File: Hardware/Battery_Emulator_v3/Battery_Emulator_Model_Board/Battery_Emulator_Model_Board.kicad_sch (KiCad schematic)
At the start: 43 parts, among them J1 Vin, J10 Conn_01x05, J11 Conn_01x05, J12 Conn_01x05, J13 Conn_01x05, J14 Conn_01x05, J15 Conn_01x05, J16 Conn_01x05, J17 Conn_01x05, J2 USB4105-GF-A-060, J3 Conn_01x05, J5 Conn_01x05, J6 Conn_01x05, J7 Conn_01x05, J8 Conn_01x05, J9 Conn_01x05, U1 ATmega328PB-A, U2 KA78M05_TO252, U3 FT230XS-R, U4 74AHC2G125DP,125, Y1 Crystal_GND24

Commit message: Hardware Update
Finished the Model Board PCB
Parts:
- added TP4: GND, TestPoint:TestPoint_Pad_D2.5mm, symbol Connector:TestPoint
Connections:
- net GND: now also TP4.1
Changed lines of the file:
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@@
   (junction (at 49.53 21.59) (diameter 0) (color 0 0 0 0)
   )
+  (junction (at 107.315 36.83) (diameter 0) (color 0 0 0 0)
+  )
   (junction (at 77.47 113.03) (diameter 0) (color 0 0 0 0)
   )
@@
         )
       )
+    )
+  )
+  (symbol (lib_id "Connector:TestPoint") (at 107.315 36.83 180) (unit 1)
+    (in_bom yes) (on_board yes) (dnp no) (fields_autoplaced)
+    (property "Reference" "TP4" (at 109.855 38.862 0)
+      (effects (font (size 1.27 1.27)) (justify right))
+    )
+    (property "Value" "GND" (at 109.855 41.402 0)
+      (effects (font (size 1.27 1.27)) (justify right))
+    )
+    (property "Footprint" "TestPoint:TestPoint_Pad_D2.5mm" (at 102.235 36.83 0)
+      (effects (font (size 1.27 1.27)) hide)
+    )
+    (property "Datasheet" "~" (at 102.235 36.83 0)
+      (effects (font (size 1.27 1.27)) hide)
+    )
+    (pin "1")
+    (instances
+      (project "Battery_Emulator_Model_Board"
+        (path "/148b0eed-bd25-41de-bd25-36484a90c6fc"
+          (reference "TP4") (unit 1)
+        )
+      )
+      (project "Battery_Emulator"
+        (path "/bb7641ff-0dfd-4f4a-b3be-57afbbb9fdac/86a0f187-fc20-4f8c-b621-2752c8234446"
+          (reference "TP2") (unit 1)
+        )
+        (path "/bb7641ff-0dfd-4f4a-b3be-57afbbb9fdac/b6a9662d-5d6a-45a2-997c-bd44d3cd27c8"
+          (reference "TP3") (unit 1)
+        )
+        (path "/bb7641ff-0dfd-4f4a-b3be-57afbbb9fdac"
+          (reference "TP10") (unit 1)
+        )
+      )

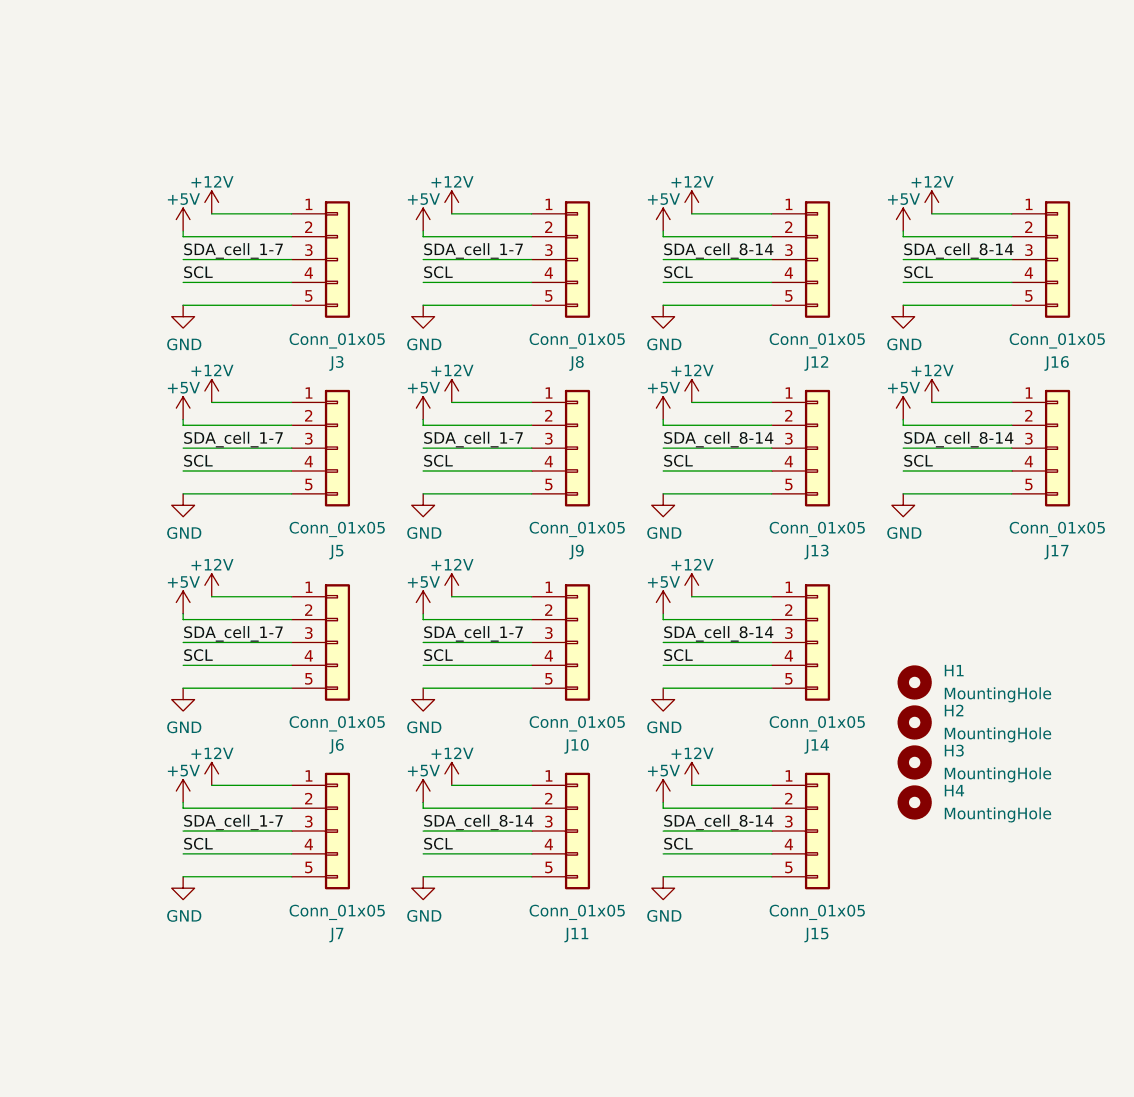
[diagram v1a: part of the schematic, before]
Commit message: Updated mother board + cell PCB
Made +12V trace on mother board 2mm so it can withstand 2A. Improved routing a bit. Changed pinheader to pinsocket on motherboard and pinsocket to pinheader on cell PCB. Mother board is nearly finished, Cell PCB is not finished.
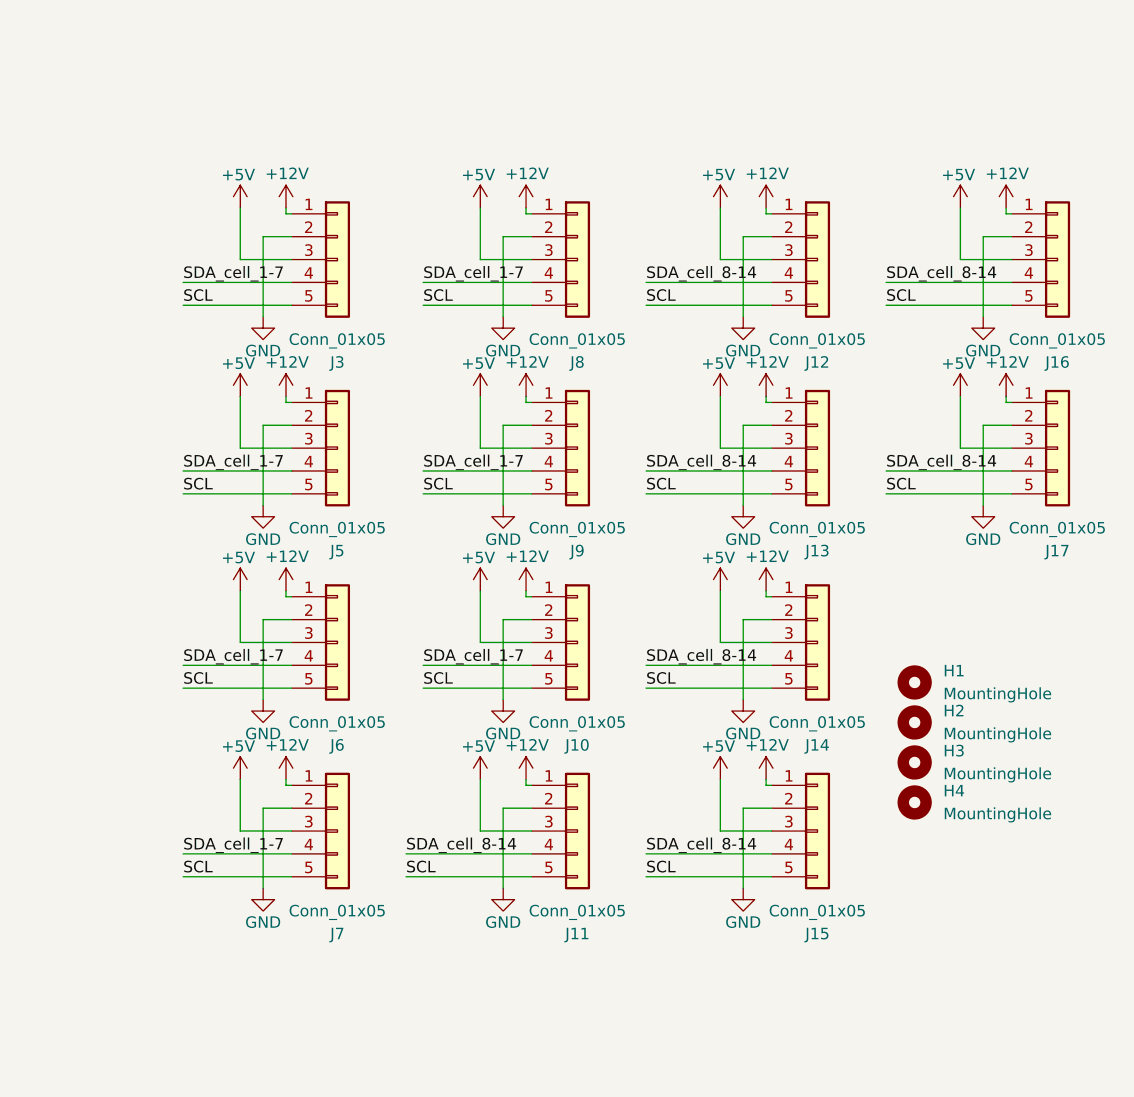
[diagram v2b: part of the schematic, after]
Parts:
- J10, J11, J12, J13, J14, J15, J16, J17, J3, J5, J6, J7, J8, J9: footprint Connector_PinHeader_2.54mm:PinHeader_1x05_P2.54mm_Horizontal -> Connector_PinSocket_2.54mm:PinSocket_1x05_P2.54mm_Horizontal
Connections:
- net +5V: now also J10.3 (Pin_3), J11.3 (Pin_3), J12.3 (Pin_3), J13.3 (Pin_3), J14.3 (Pin_3), J15.3 (Pin_3), J16.3 (Pin_3), J17.3 (Pin_3), J3.3 (Pin_3), J5.3 (Pin_3), J6.3 (Pin_3), J7.3 (Pin_3), J8.3 (Pin_3), J9.3 (Pin_3); no longer J10.2 (Pin_2), J11.2 (Pin_2), J12.2 (Pin_2), J13.2 (Pin_2), J14.2 (Pin_2), J15.2 (Pin_2), J16.2 (Pin_2), J17.2 (Pin_2), J3.2 (Pin_2), J5.2 (Pin_2), J6.2 (Pin_2), J7.2 (Pin_2), J8.2 (Pin_2), J9.2 (Pin_2)
- net GND: now also J10.2 (Pin_2), J11.2 (Pin_2), J12.2 (Pin_2), J13.2 (Pin_2), J14.2 (Pin_2), J15.2 (Pin_2), J16.2 (Pin_2), J17.2 (Pin_2), J3.2 (Pin_2), J5.2 (Pin_2), J6.2 (Pin_2), J7.2 (Pin_2), J8.2 (Pin_2), J9.2 (Pin_2); no longer J10.5 (Pin_5), J11.5 (Pin_5), J12.5 (Pin_5), J13.5 (Pin_5), J14.5 (Pin_5), J15.5 (Pin_5), J16.5 (Pin_5), J17.5 (Pin_5), J3.5 (Pin_5), J5.5 (Pin_5), J6.5 (Pin_5), J7.5 (Pin_5), J8.5 (Pin_5), J9.5 (Pin_5)
- net SCL: now also J10.5 (Pin_5), J11.5 (Pin_5), J12.5 (Pin_5), J13.5 (Pin_5), J14.5 (Pin_5), J15.5 (Pin_5), J16.5 (Pin_5), J17.5 (Pin_5), J3.5 (Pin_5), J5.5 (Pin_5), J6.5 (Pin_5), J7.5 (Pin_5), J8.5 (Pin_5), J9.5 (Pin_5); no longer J10.4 (Pin_4), J11.4 (Pin_4), J12.4 (Pin_4), J13.4 (Pin_4), J14.4 (Pin_4), J15.4 (Pin_4), J16.4 (Pin_4), J17.4 (Pin_4), J3.4 (Pin_4), J5.4 (Pin_4), J6.4 (Pin_4), J7.4 (Pin_4), J8.4 (Pin_4), J9.4 (Pin_4)
- net SDA_cell_1-7: now also J10.4 (Pin_4), J3.4 (Pin_4), J5.4 (Pin_4), J6.4 (Pin_4), J7.4 (Pin_4), J8.4 (Pin_4), J9.4 (Pin_4); no longer J10.3 (Pin_3), J3.3 (Pin_3), J5.3 (Pin_3), J6.3 (Pin_3), J7.3 (Pin_3), J8.3 (Pin_3), J9.3 (Pin_3)
- net SDA_cell_8-14: now also J11.4 (Pin_4), J12.4 (Pin_4), J13.4 (Pin_4), J14.4 (Pin_4), J15.4 (Pin_4), J16.4 (Pin_4), J17.4 (Pin_4); no longer J11.3 (Pin_3), J12.3 (Pin_3), J13.3 (Pin_3), J14.3 (Pin_3), J15.3 (Pin_3), J16.3 (Pin_3), J17.3 (Pin_3)
